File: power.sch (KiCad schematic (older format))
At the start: 32 parts, among them U1 ICE40HX4K-TQ144, U6 TLV62568APDRLR, U7 TLV62568APDRLR

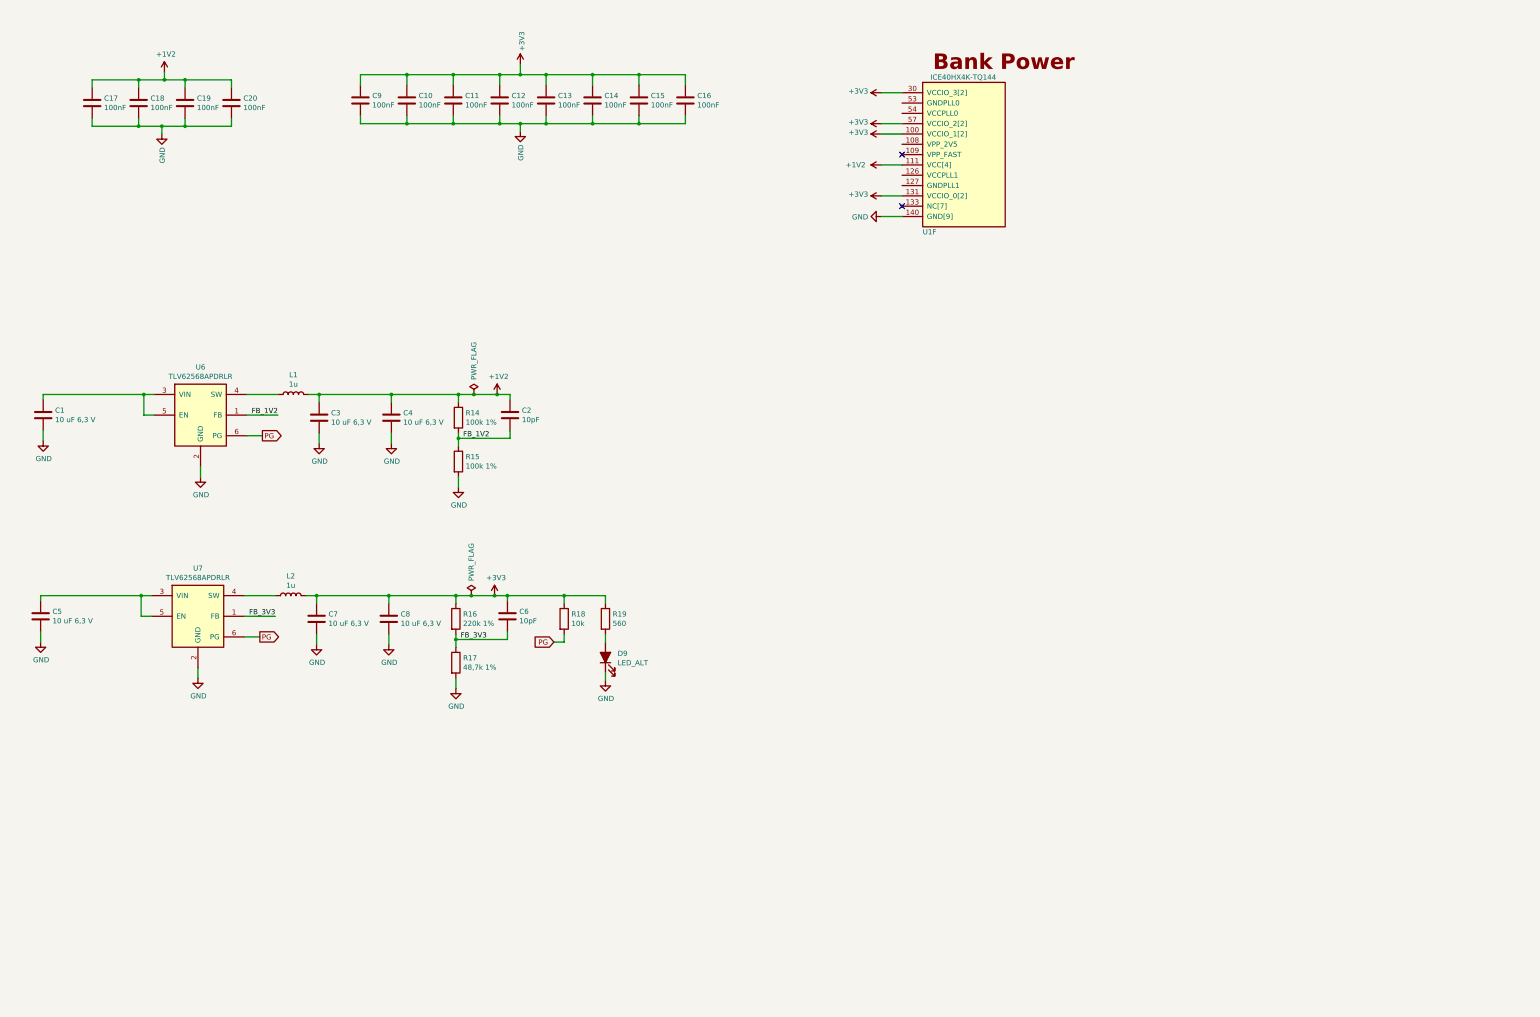
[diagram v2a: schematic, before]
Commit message: Added switches, added 5 V rail and 17 V input(with filtering). Power is mostly done.
Also added a first version of buffers to ftdi chip. I'll change the evtl.

Started to route power section.
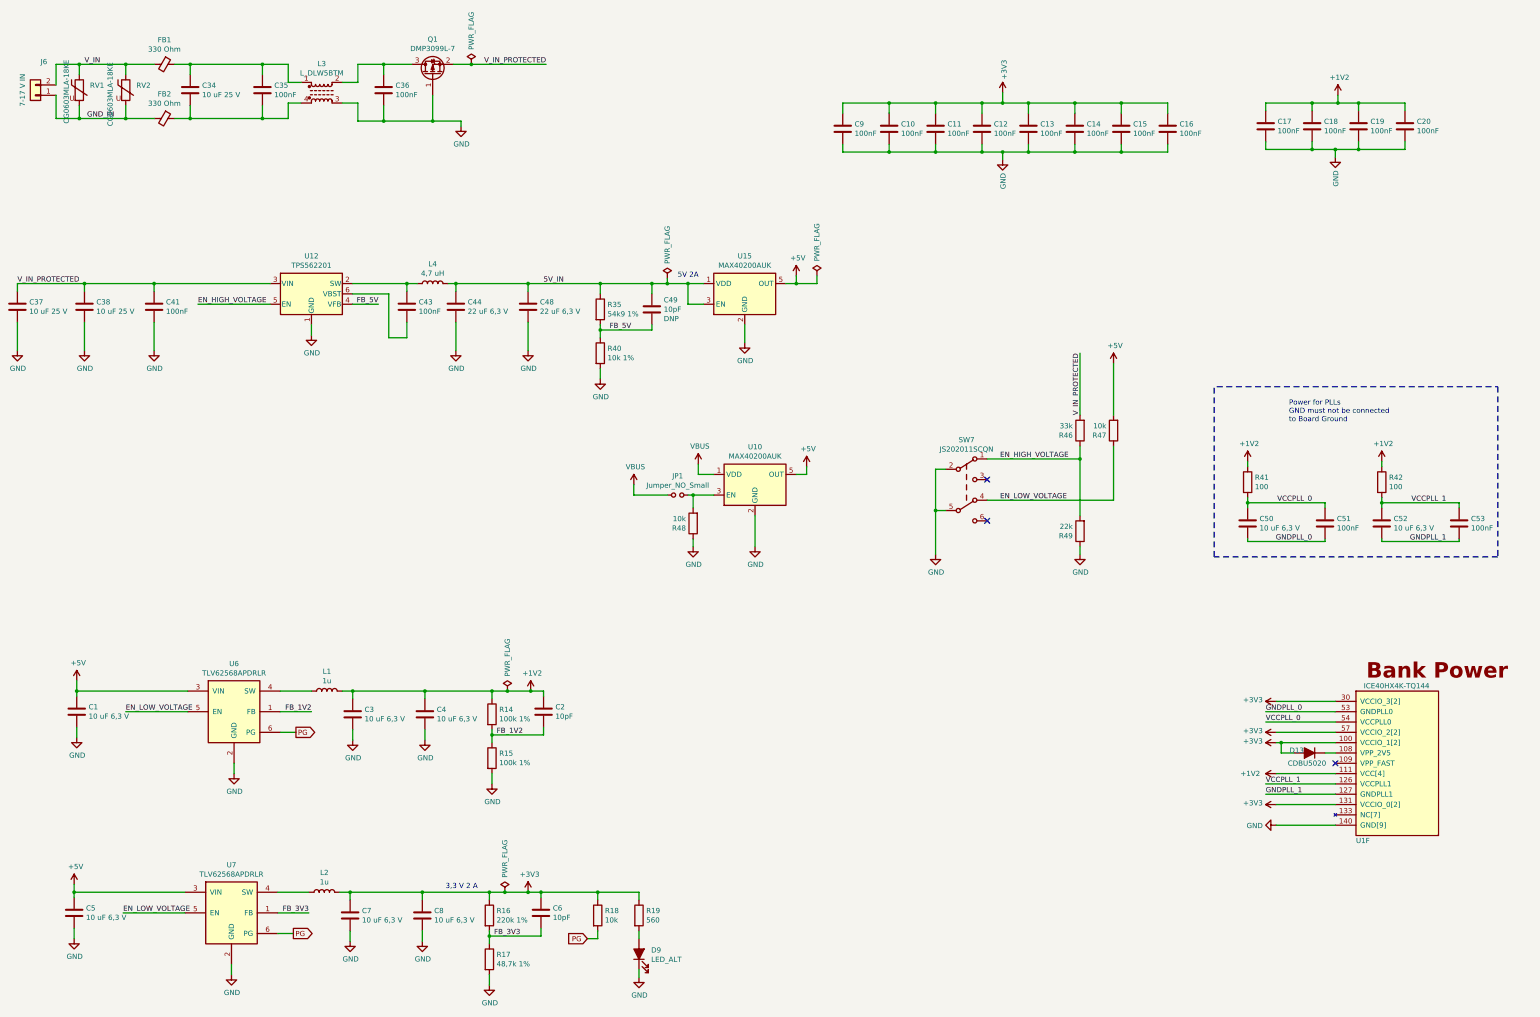
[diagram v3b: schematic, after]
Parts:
- added C34, C37, C38: 10 uF 25 V, Capacitor_SMD:C_0805_2012Metric, symbol Device:C
- added C35, C36, C41, C43, C51, C53: 100nF, Capacitor_SMD:C_0603_1608Metric, symbol Device:C
- added C44, C48: 22 uF 6,3 V, Capacitor_SMD:C_0603_1608Metric, symbol Device:C
- added C49: 10pF, Capacitor_SMD:C_0603_1608Metric, symbol Device:C
- added C50, C52: 10 uF 6,3 V, Capacitor_SMD:C_0603_1608Metric, symbol Device:C
- added D13: CDBU5020, Diode_SMD:D_0603_1608Metric, symbol Device:D_ALT
- added FB1, FB2: 330 Ohm, Resistor_SMD:R_0805_2012Metric, symbol Device:Ferrite_Bead_Small
- added J6: 7-17 V IN, TerminalBlock:TerminalBlock_bornier-2_P5.08mm, symbol Connector_Generic:Conn_01x02
- added JP1: Jumper_NO_Small, Connector_PinHeader_2.54mm:PinHeader_1x02_P2.54mm_Vertical, symbol Device:Jumper_NO_Small
- added L3: L_DLW5BTM, footprints:DLW5BTM_5.00x5.00mm_footprint, symbol l_dlw5btm:L_DLW5BTM
- added L4: 4,7 uH, Inductor_SMD:L_Taiyo-Yuden_NR-50xx, symbol Device:L
- added Q1: DMP3099L-7, Package_TO_SOT_SMD:SOT-23, symbol Device:Q_PMOS_GSD
- added R35: 54k9 1%, Resistor_SMD:R_0603_1608Metric, symbol Device:R
- added R40: 10k 1%, Resistor_SMD:R_0603_1608Metric, symbol Device:R
- added R41, R42: 100, Resistor_SMD:R_0603_1608Metric, symbol Device:R
- added R46: 33k, Resistor_SMD:R_0603_1608Metric, symbol Device:R
- added R47, R48: 10k, Resistor_SMD:R_0603_1608Metric, symbol Device:R
- added R49: 22k, Resistor_SMD:R_0603_1608Metric, symbol Device:R
- added RV1, RV2: CG0603MLA-18KE, Resistor_SMD:R_0603_1608Metric, symbol Device:Varistor
- added SW7: JS202011SCQN, footprints:SW_SLIDE_DPDT_Slide_CK_JS202011SCQN_W3mm_P2.5mm_footprint, symbol sw_dpdt:SW_DPDT
- added U10, U15: MAX40200AUK, Package_TO_SOT_SMD:SOT-23-5, symbol Analog_Switch:MAX40200AUK
- added U12: TPS562201, Package_TO_SOT_SMD:SOT-23-6, symbol Regulator_Switching:TPS562200
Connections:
- net +1V2: now also R41.1, R42.1
- net +3V3: now also D13.2 (A)
- net GND: now also C36.2, C37.2, C38.2, C41.2, C44.2, C48.2, L3.3, Q1.1 (G), R40.2, R48.1, R49.1, SW7.2 (B), SW7.5 (B), U10.2 (GND), U12.1 (GND), U15.2 (GND)
- net at U1.108 (VPP_2V5): now also D13.1 (K)
- net VCCPLL_1: now reaches U1.126 (VCCPLL1)
- net VCCPLL_1: now also C52.1, C53.1, R42.2
- net GNDPLL_1: now reaches U1.127 (GNDPLL1)
- net GNDPLL_1: now also C52.2, C53.2
- net GNDPLL_0: now reaches U1.53 (GNDPLL0)
- net GNDPLL_0: now also C50.2, C51.2
- net VCCPLL_0: now reaches U1.54 (VCCPLL0)
- net VCCPLL_0: now also C50.1, C51.1, R41.2
- net +5V: now reaches C1.1, U6.3 (VIN)
- net +5V: now also C5.1, U7.3 (VIN), R47.2, U10.5 (OUT), U15.5 (OUT); no longer U6.5 (EN)
- new net: JP1.2, R48.2, U10.3 (EN)
- new net: C43.1, L4.1, U12.2 (SW)
- new net: C43.2, U12.6 (VBST)
- new net: C34.1, C35.1, FB1.1, L3.1
- new net: C34.2, C35.2, FB2.1, L3.4
- new net: C36.1, L3.2, Q1.3 (D)
- new net 5V_IN: C44.1, C48.1, C49.1, L4.2, R35.1, U15.1 (VDD), U15.3 (EN)
- new net EN_HIGH_VOLTAGE: R46.1, R49.2, SW7.1 (A), U12.5 (EN)
- new net EN_LOW_VOLTAGE: R47.1, SW7.4 (A), U6.5 (EN), U7.5 (EN)
- new net FB_5V: C49.2, R35.2, R40.1, U12.4 (VFB)
- new net GND_IN: FB2.2, J6.1 (Pin_1), RV1.2, RV2.2
- new net VBUS: JP1.1, U10.1 (VDD)
- new net V_IN: FB1.2, J6.2 (Pin_2), RV1.1, RV2.1
- new net V_IN_PROTECTED: C37.1, C38.1, C41.1, Q1.2 (S), R46.2, U12.3 (VIN)
- no-connect marks 2 -> 3
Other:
- note added: "3,3 V 2 A"
- note added: "5V 2A"
- note added: "Power for PLLs\nGND must not be connected\nto Board Ground"
- moved on the sheet: C1, C10, C11, C12, C13, C14, C15, C16, C17, C18, C19, C2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

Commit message: Continued on Power PCB design
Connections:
- net V_IN_FILTERED: now reaches C34.1, C35.1, FB1.1, L3.1
- net GND_IN_FILTERED: now reaches C34.2, C35.2, FB2.1, L3.4
- net V_IN_CHOKE: now reaches C36.1, L3.2, Q1.3 (D)
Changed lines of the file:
@@
 Connection ~ 1725 1075
-$Comp
-L l_dlw5btm:L_DLW5BTM L3
-U 1 1 5CE854C4
-P 3625 1350
-F 0 "L3" H 3625 1631 50  0000 C CNN
-F 1 "L_DLW5BTM" H 3625 1540 50  0000 C CNN
-F 2 "footprints:DLW5BTM_5.00x5.00mm_footprint" H 3625 1350 50  0001 C CNN
-F 3 "https://www.murata.com/en-us/products/productdata/8796761587742/EFLC0025.pdf" H 3625 1350 50  0001 C CNN
-F 4 "Murata Electronics North America" H 3625 1350 50  0001 C CNN "Mfg Name"
-F 5 "DLW5BTM251SQ2L" H 3625 1350 50  0001 C CNN "Mfg Part Num"
-F 6 "490-11111-1-ND" H 3625 1350 50  0001 C CNN "Digikey"
-F 7 "CMC 5A 2LN 250 OHM SMD" H 3625 1350 50  0001 C CNN "Description"
-	1    3625 1350
-	1    0    0    -1
-$EndComp
 $Comp
 L Device:C C43
@@
 	3825 1450 3975 1450
 Connection ~ 4225 1625
+Text Label 2475 1075 0    50   ~ 0
+V_IN_FILTERED
+Text Label 2400 1600 0    50   ~ 0
+GND_IN_FILTERED
+Text Label 4000 1075 0    50   ~ 0
+V_IN_CHOKE
+$Comp
+L l_dlw5btm:L_DLW5BTM L3
+U 1 1 5CE854C4
+P 3625 1350
+F 0 "L3" H 3625 1631 50  0000 C CNN
+F 1 "L_DLW5BTM" H 3625 1540 50  0000 C CNN
+F 2 "footprints:DLW5BTM_5.00x5.00mm_footprint" H 3625 1350 50  0001 C CNN
+F 3 "https://www.murata.com/en-us/products/productdata/8796761587742/EFLC0025.pdf" H 3625 1350 50  0001 C CNN
+F 4 "Murata Electronics North America" H 3625 1350 50  0001 C CNN "Mfg Name"
+F 5 "DLW5BTM251SQ2L" H 3625 1350 50  0001 C CNN "Mfg Part Num"
+F 6 "490-11111-1-ND" H 3625 1350 50  0001 C CNN "Digikey"
+F 7 "CMC 5A 2LN 250 OHM SMD" H 3625 1350 50  0001 C CNN "Description"
+	1    3625 1350
+	1    0    0    -1
+$EndComp
 $EndSCHEMATC

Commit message: Continued with routing
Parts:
- added C83, C84: 10 uF 6,3 V, Capacitor_SMD:C_0603_1608Metric, symbol Device:C
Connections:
- net +1V2: now also C83.1
- net +3V3: now also C84.1
- net EN_HIGH_VOLTAGE: now also SW7.4 (A); no longer SW7.1 (A)
- net EN_LOW_VOLTAGE: now also SW7.1 (A); no longer SW7.4 (A)
- net GND: now also C83.2, C84.2
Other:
- moved on the sheet: C10, C11, C12, C13, C14, C15, C16, C17, C18, C19, C20, C9
